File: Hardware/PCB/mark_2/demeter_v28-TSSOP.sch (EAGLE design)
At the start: 68 parts, among them IC1 4050, IC2 LM1117-5.0, IC3 LM1117-3.3, IC5 MCP3424T, IC6 MCP23017SO, IC8 ATMEGA32U4-AU, Q1 IRLML6402, Q2 IRLML6402, Q3 IRLML6402, Q4 IRLML6402, Q5 IRLML6402, Q6 IRLML6402

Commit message: 
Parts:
- R3, R6, R8: value (none) -> 10k
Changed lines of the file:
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@@
 <?xml version="1.0" encoding="utf-8"?>
 <!DOCTYPE eagle SYSTEM "eagle.dtd">
-<eagle version="6.1">
+<eagle version="6.2">
 <drawing>
 <settings>
@@
 <part name="R4" library="mark_2" deviceset="R-EU_" device="R0805"/>
 <part name="GND20" library="mark_2" deviceset="GND" device=""/>
-<part name="R8" library="mark_2" deviceset="R-EU_" device="R0805"/>
+<part name="R8" library="mark_2" deviceset="R-EU_" device="R0805" value="10k"/>
 <part name="D2" library="mark_2" deviceset="MBR0520" device="" value=""/>
 <part name="P+6" library="mark_2" deviceset="+5V" device=""/>
@@
 <part name="JK3" library="mark_2" deviceset="AUDIO-JACK2" device="PTH"/>
 <part name="GND17" library="mark_2" deviceset="GND" device=""/>
-<part name="R6" library="mark_2" deviceset="R-EU_" device="R0805"/>
+<part name="R6" library="mark_2" deviceset="R-EU_" device="R0805" value="10k"/>
 <part name="GND18" library="mark_2" deviceset="GND" device=""/>
 <part name="D6" library="mark_2" deviceset="MBR0520" device="" value=""/>
@@
 <part name="GND8" library="mark_2" deviceset="GND" device=""/>
 <part name="JP1" library="mark_2" deviceset="AVR-ISP-6" device=""/>
-<part name="R3" library="mark_2" deviceset="R-EU_" device="R0805"/>
+<part name="R3" library="mark_2" deviceset="R-EU_" device="R0805" value="10k"/>
 <part name="P+14" library="mark_2" deviceset="+5V" device=""/>
 <part name="P+15" library="mark_2" deviceset="+5V" device=""/>

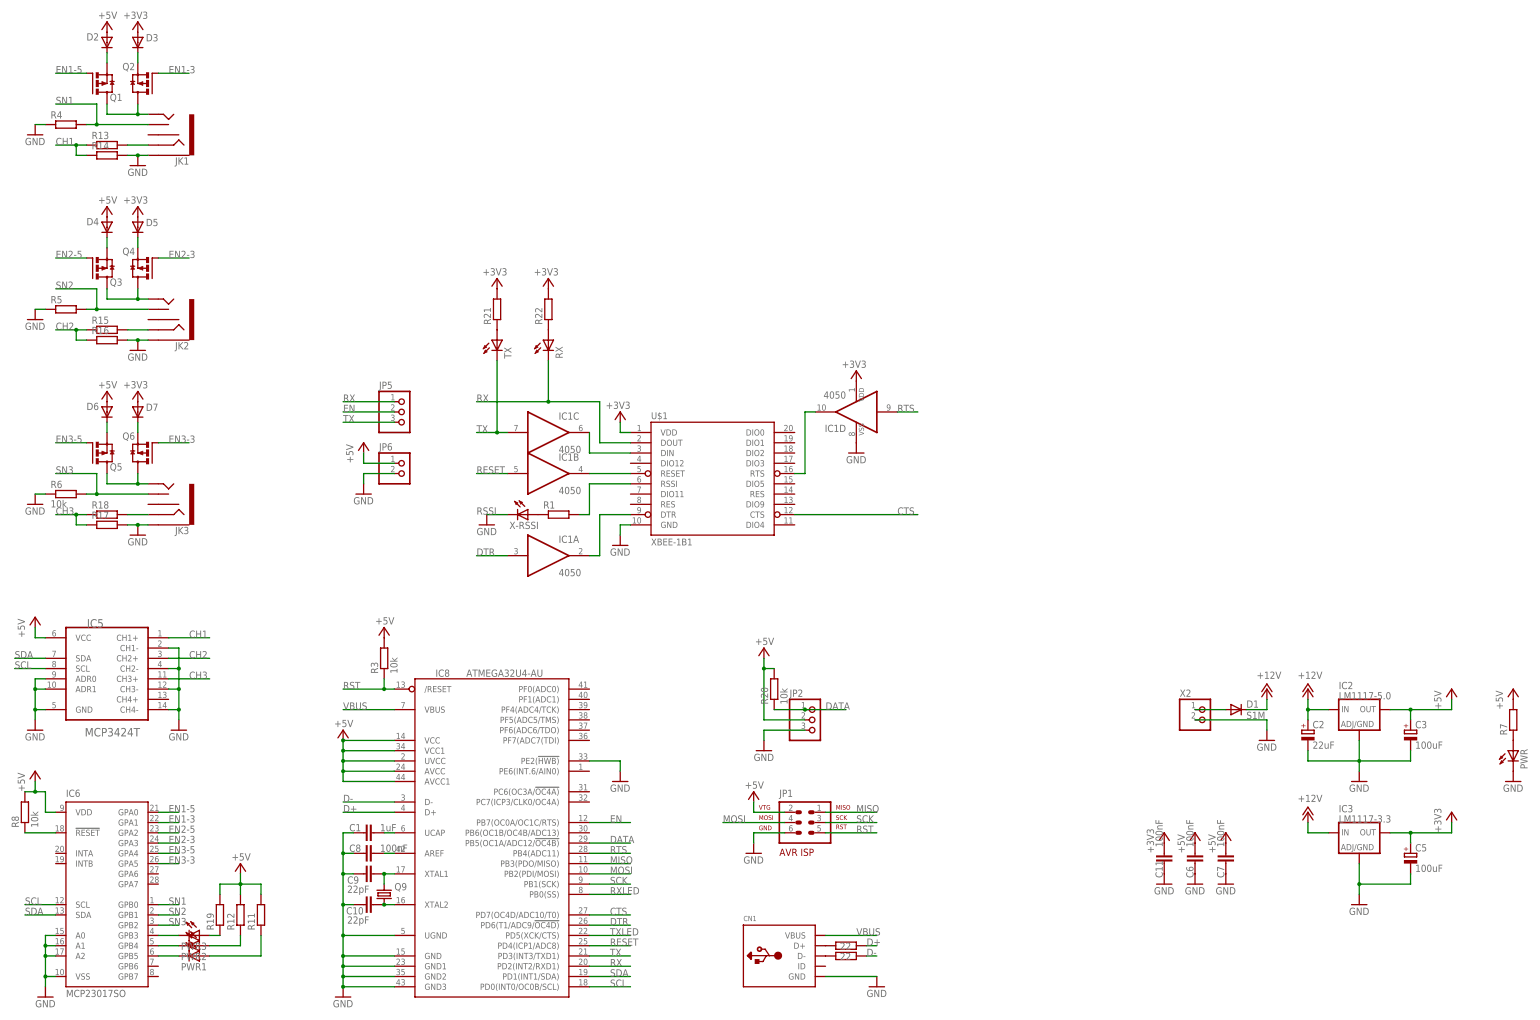
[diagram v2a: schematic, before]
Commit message: 
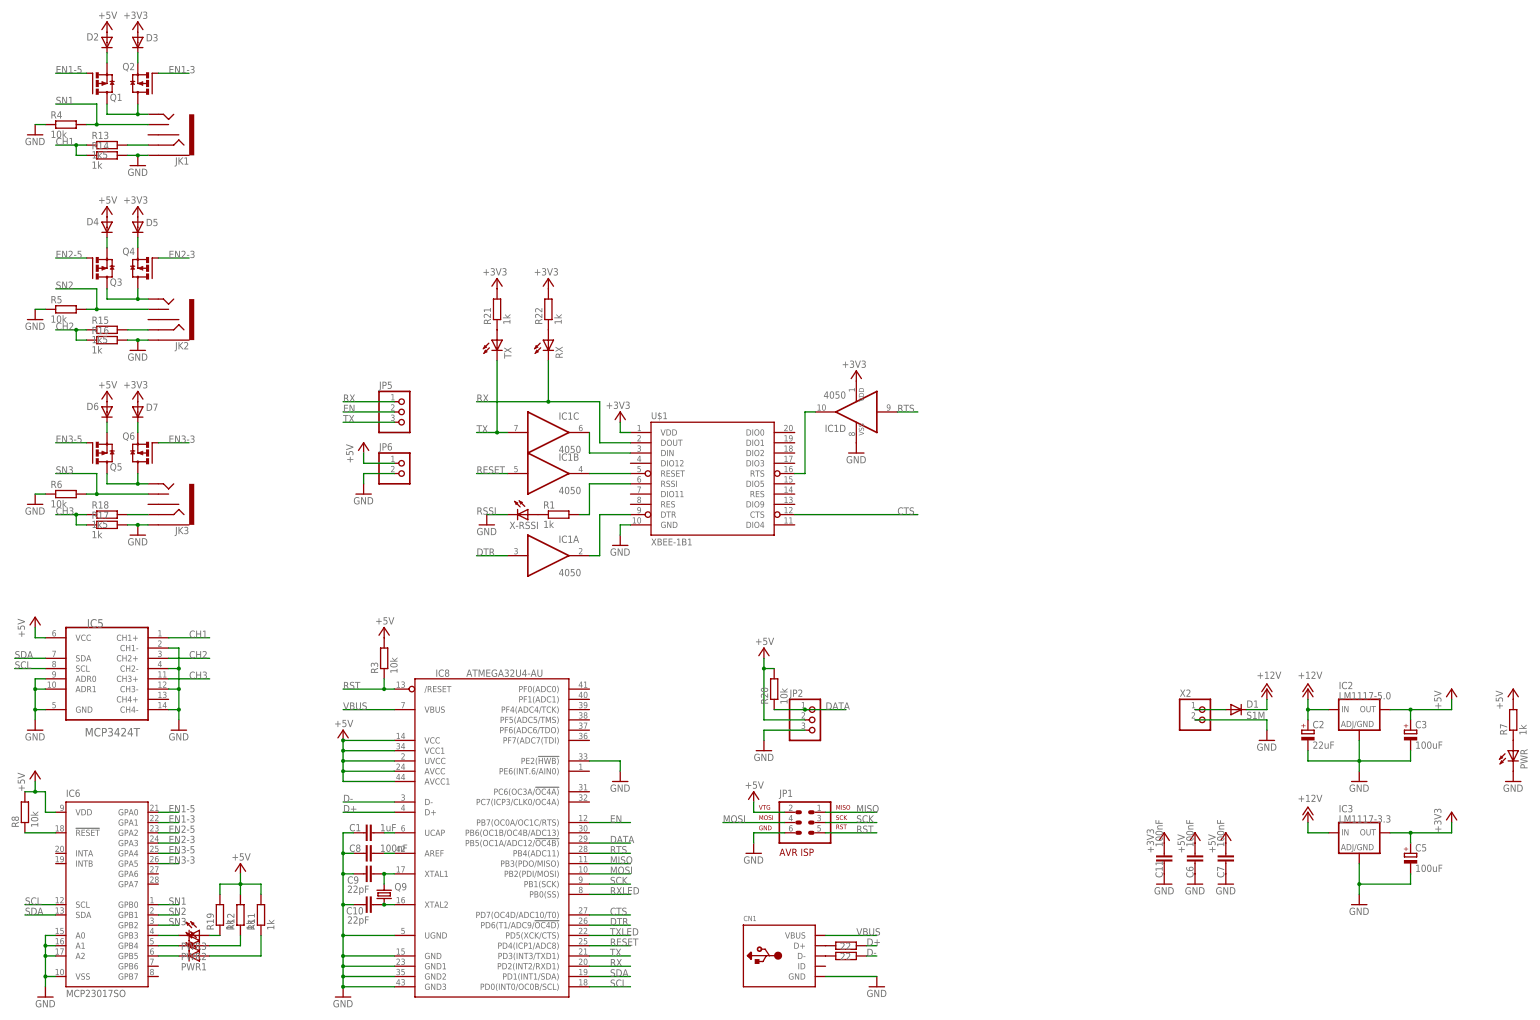
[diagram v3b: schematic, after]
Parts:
- R1, R11, R12, R14, R16, R17, R19, R21, R22, R7: value (none) -> 1k
- R13, R15, R18: value (none) -> 1k5
- R4, R5: value (none) -> 10k
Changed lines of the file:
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@@
 <part name="IC1" library="mark_2" deviceset="4050" device="D" value="4050"/>
 <part name="X-RSSI" library="mark_2" deviceset="LED" device="0805"/>
-<part name="R1" library="mark_2" deviceset="R-EU_" device="R0805"/>
+<part name="R1" library="mark_2" deviceset="R-EU_" device="R0805" value="1k"/>
 <part name="U$1" library="mark_2" deviceset="XBEE-1" device="B1"/>
 <part name="+3V2" library="mark_2" deviceset="+3V3" device=""/>
@@
 <part name="JK1" library="mark_2" deviceset="AUDIO-JACK2" device="PTH"/>
 <part name="GND16" library="mark_2" deviceset="GND" device=""/>
-<part name="R4" library="mark_2" deviceset="R-EU_" device="R0805"/>
+<part name="R4" library="mark_2" deviceset="R-EU_" device="R0805" value="10k"/>
 <part name="GND20" library="mark_2" deviceset="GND" device=""/>
 <part name="R8" library="mark_2" deviceset="R-EU_" device="R0805" value="10k"/>
@@
 <part name="JK2" library="mark_2" deviceset="AUDIO-JACK2" device="PTH"/>
 <part name="GND9" library="mark_2" deviceset="GND" device=""/>
-<part name="R5" library="mark_2" deviceset="R-EU_" device="R0805"/>
+<part name="R5" library="mark_2" deviceset="R-EU_" device="R0805" value="10k"/>
 <part name="GND11" library="mark_2" deviceset="GND" device=""/>
 <part name="D4" library="mark_2" deviceset="MBR0520" device="" value=""/>
@@
 <part name="R9" library="mark_2" deviceset="R-EU_" device="R0805" value="22"/>
 <part name="R10" library="mark_2" deviceset="R-EU_" device="R0805" value="22"/>
-<part name="R13" library="mark_2" deviceset="R-EU_" device="R0805"/>
-<part name="R14" library="mark_2" deviceset="R-EU_" device="R0805"/>
-<part name="R15" library="mark_2" deviceset="R-EU_" device="R0805"/>
-<part name="R16" library="mark_2" deviceset="R-EU_" device="R0805"/>
-<part name="R17" library="mark_2" deviceset="R-EU_" device="R0805"/>
-<part name="R18" library="mark_2" deviceset="R-EU_" device="R0805"/>
+<part name="R13" library="mark_2" deviceset="R-EU_" device="R0805" value="1k5"/>
+<part name="R14" library="mark_2" deviceset="R-EU_" device="R0805" value="1k"/>
+<part name="R15" library="mark_2" deviceset="R-EU_" device="R0805" value="1k5"/>
+<part name="R16" library="mark_2" deviceset="R-EU_" device="R0805" value="1k"/>
+<part name="R17" library="mark_2" deviceset="R-EU_" device="R0805" value="1k"/>
+<part name="R18" library="mark_2" deviceset="R-EU_" device="R0805" value="1k5"/>
 <part name="FRAME1" library="mark_2" deviceset="DINA3_L" device=""/>
 <part name="GND28" library="mark_2" deviceset="GND" device=""/>
@@
 <part name="GND10" library="mark_2" deviceset="GND" device=""/>
 <part name="P+5" library="mark_2" deviceset="+5V" device=""/>
-<part name="R7" library="mark_2" deviceset="R-EU_" device="R0805"/>
+<part name="R7" library="mark_2" deviceset="R-EU_" device="R0805" value="1k"/>
 <part name="PWR" library="mark_2" deviceset="LED" device="0805"/>
 <part name="GND7" library="mark_2" deviceset="GND" device=""/>
@@
 <part name="GND21" library="mark_2" deviceset="GND" device=""/>
 <part name="+3V7" library="mark_2" deviceset="+3V3" device=""/>
-<part name="R11" library="mark_2" deviceset="R-EU_" device="R0805"/>
+<part name="R11" library="mark_2" deviceset="R-EU_" device="R0805" value="1k"/>
 <part name="PWR1" library="mark_2" deviceset="LED" device="0805"/>
 <part name="P+17" library="mark_2" deviceset="+5V" device=""/>
-<part name="R12" library="mark_2" deviceset="R-EU_" device="R0805"/>
+<part name="R12" library="mark_2" deviceset="R-EU_" device="R0805" value="1k"/>
 <part name="PWR2" library="mark_2" deviceset="LED" device="0805"/>
 <part name="PWR3" library="mark_2" deviceset="LED" device="0805"/>
-<part name="R19" library="mark_2" deviceset="R-EU_" device="R0805"/>
+<part name="R19" library="mark_2" deviceset="R-EU_" device="R0805" value="1k"/>
 <part name="P+18" library="mark_2" deviceset="+5V" device=""/>
 <part name="GND25" library="mark_2" deviceset="GND" device=""/>
@@
 <part name="JP2" library="mark_2" deviceset="PINHD-1X3" device="180"/>
 <part name="TX" library="mark_2" deviceset="LED" device="0805"/>
-<part name="R21" library="mark_2" deviceset="R-EU_" device="R0805"/>
+<part name="R21" library="mark_2" deviceset="R-EU_" device="R0805" value="1k"/>
 <part name="RX" library="mark_2" deviceset="LED" device="0805"/>
-<part name="R22" library="mark_2" deviceset="R-EU_" device="R0805"/>
+<part name="R22" library="mark_2" deviceset="R-EU_" device="R0805" value="1k"/>
 <part name="+3V9" library="mark_2" deviceset="+3V3" device=""/>
 <part name="+3V8" library="mark_2" deviceset="+3V3" device=""/>

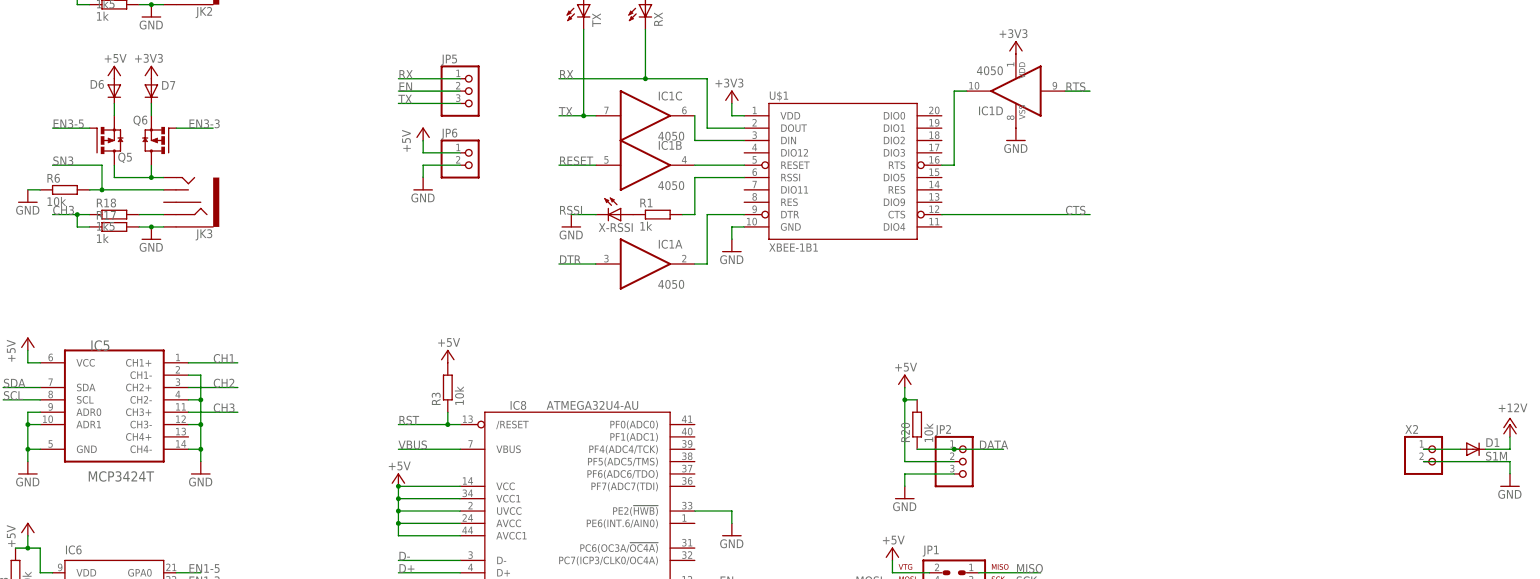
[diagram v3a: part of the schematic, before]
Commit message: 
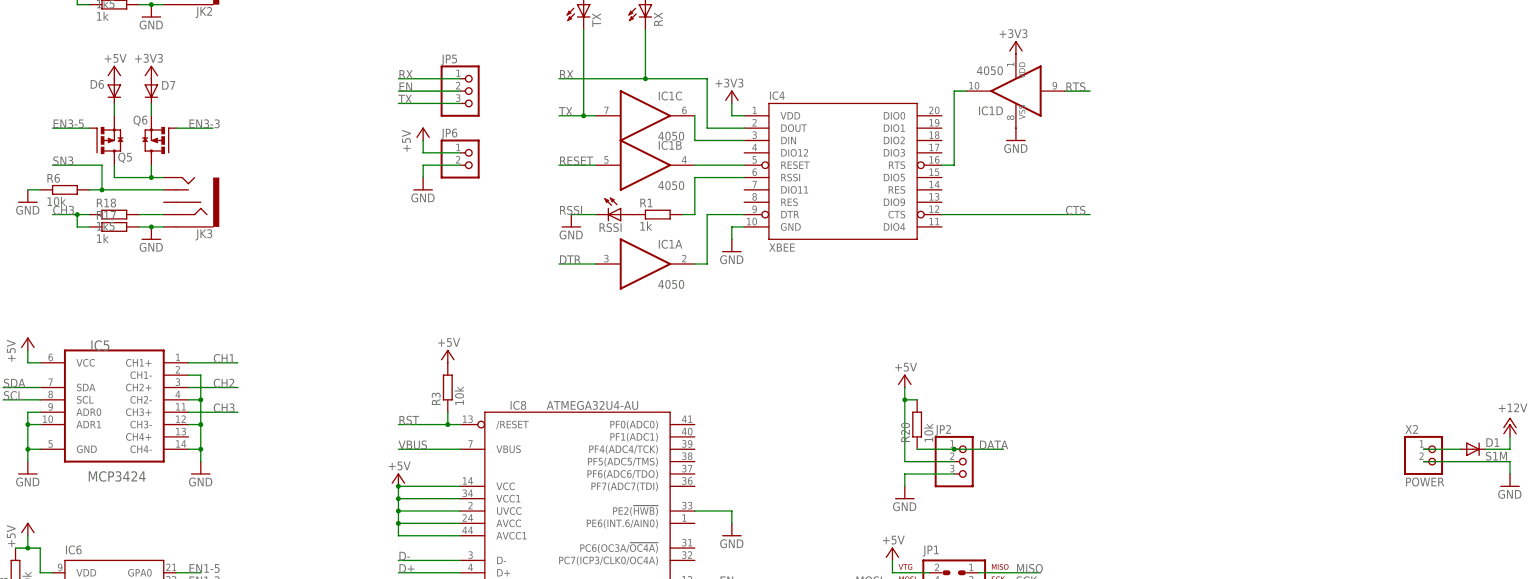
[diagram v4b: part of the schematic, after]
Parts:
- IC4: value XBEE-1B1 -> XBEE
- IC5: value MCP3424T -> MCP3424
- JP1: value AVR-ISP-6 -> AVR-ISP
- X2: value (none) -> POWER
- renumbered U$1 to IC4, X-RSSI to RSSI
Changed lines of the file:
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@@
 <?xml version="1.0" encoding="utf-8"?>
 <!DOCTYPE eagle SYSTEM "eagle.dtd">
-<eagle version="6.2">
+<eagle version="6.1">
 <drawing>
 <settings>
@@
 <parts>
 <part name="IC1" library="mark_2" deviceset="4050" device="D" value="4050"/>
-<part name="X-RSSI" library="mark_2" deviceset="LED" device="0805"/>
+<part name="RSSI" library="mark_2" deviceset="LED" device="0805"/>
 <part name="R1" library="mark_2" deviceset="R-EU_" device="R0805" value="1k"/>
-<part name="U$1" library="mark_2" deviceset="XBEE-1" device="B1"/>
+<part name="IC4" library="mark_2" deviceset="XBEE-1" device="B1" value="XBEE"/>
 <part name="+3V2" library="mark_2" deviceset="+3V3" device=""/>
 <part name="GND3" library="mark_2" deviceset="GND" device=""/>
@@
 <part name="Q1" library="mark_2" deviceset="IRLML6402" device=""/>
 <part name="GND13" library="mark_2" deviceset="GND" device=""/>
-<part name="IC5" library="mark_2" deviceset="MCP3424" device="T"/>
+<part name="IC5" library="mark_2" deviceset="MCP3424" device="T" value="MCP3424"/>
 <part name="P+10" library="mark_2" deviceset="+5V" device=""/>
 <part name="GND14" library="mark_2" deviceset="GND" device=""/>
@@
 <part name="P+13" library="mark_2" deviceset="+5V" device=""/>
 <part name="GND8" library="mark_2" deviceset="GND" device=""/>
-<part name="JP1" library="mark_2" deviceset="AVR-ISP-6" device=""/>
+<part name="JP1" library="mark_2" deviceset="AVR-ISP-6" device="" value="AVR-ISP"/>
 <part name="R3" library="mark_2" deviceset="R-EU_" device="R0805" value="10k"/>
 <part name="P+14" library="mark_2" deviceset="+5V" device=""/>
@@
 <part name="FRAME1" library="mark_2" deviceset="DINA3_L" device=""/>
 <part name="GND28" library="mark_2" deviceset="GND" device=""/>
-<part name="X2" library="mark_2" deviceset="W237-102" device=""/>
+<part name="X2" library="mark_2" deviceset="W237-102" device="" value="POWER"/>
 <part name="GND24" library="mark_2" deviceset="GND" device=""/>
 <part name="JP5" library="mark_2" deviceset="PINHD-1X3" device="180"/>
@@
 <attribute name="VALUE" x="180.34" y="127" size="1.778" layer="96" rot="R180"/>
 </instance>
-<instance part="X-RSSI" gate="G$1" x="101.6" y="96.52" rot="R270"/>
+<instance part="RSSI" gate="G$1" x="101.6" y="96.52" rot="R270"/>
 <instance part="R1" gate="G$1" x="109.22" y="96.52"/>
-<instance part="U$1" gate="G$1" x="147.32" y="106.68"/>
+<instance part="IC4" gate="G$1" x="147.32" y="106.68"/>
 <instance part="+3V2" gate="G$1" x="124.46" y="121.92" smashed="yes">
 <attribute name="VALUE" x="127" y="124.46" size="1.778" layer="96" rot="R180"/>
@@
 <net name="GND" class="0">
 <segment>
-<pinref part="X-RSSI" gate="G$1" pin="C"/>
+<pinref part="RSSI" gate="G$1" pin="C"/>
 <pinref part="GND3" gate="1" pin="GND"/>
 <wire x1="91.44" y1="96.52" x2="96.52" y2="96.52" width="0.1524" layer="91"/>
 </segment>
 <segment>
-<pinref part="U$1" gate="G$1" pin="GND"/>
+<pinref part="IC4" gate="G$1" pin="GND"/>
 <pinref part="GND4" gate="1" pin="GND"/>
 <wire x1="124.46" y1="91.44" x2="124.46" y2="93.98" width="0.1524" layer="91"/>
@@
 <net name="+3V3" class="0">
 <segment>
-<pinref part="U$1" gate="G$1" pin="VDD"/>
+<pinref part="IC4" gate="G$1" pin="VDD"/>
 <pinref part="+3V2" gate="G$1" pin="+3V3"/>
 <wire x1="127" y1="116.84" x2="124.46" y2="116.84" width="0.1524" layer="91"/>
@@
 <net name="N$3" class="0">
 <segment>
-<pinref part="U$1" gate="G$1" pin="DIN"/>
+<pinref part="IC4" gate="G$1" pin="DIN"/>
 <wire x1="116.84" y1="116.84" x2="116.84" y2="111.76" width="0.1524" layer="91"/>
 <wire x1="116.84" y1="111.76" x2="127" y2="111.76" width="0.1524" layer="91"/>
@@
 <net name="N$4" class="0">
 <segment>
-<pinref part="U$1" gate="G$1" pin="RESET"/>
+<pinref part="IC4" gate="G$1" pin="RESET"/>
 <pinref part="IC1" gate="B" pin="O"/>
 <wire x1="116.84" y1="106.68" x2="127" y2="106.68" width="0.1524" layer="91"/>
@@
 <net name="RSSI" class="0">
 <segment>
-<pinref part="U$1" gate="G$1" pin="RSSI"/>
+<pinref part="IC4" gate="G$1" pin="RSSI"/>
 <pinref part="R1" gate="G$1" pin="2"/>
 <wire x1="127" y1="104.14" x2="116.84" y2="104.14" width="0.1524" layer="91"/>
@@
 <segment>
 <pinref part="R1" gate="G$1" pin="1"/>
-<pinref part="X-RSSI" gate="G$1" pin="A"/>
+<pinref part="RSSI" gate="G$1" pin="A"/>
 </segment>
 </net>
@@
 <wire x1="116.84" y1="86.36" x2="119.38" y2="86.36" width="0.1524" layer="91"/>
 <wire x1="119.38" y1="86.36" x2="119.38" y2="96.52" width="0.1524" layer="91"/>
-<pinref part="U$1" gate="G$1" pin="DTR"/>
+<pinref part="IC4" gate="G$1" pin="DTR"/>
 <wire x1="119.38" y1="96.52" x2="127" y2="96.52" width="0.1524" layer="91"/>
 <pinref part="IC1" gate="A" pin="O"/>
@@
 <net name="N$8" class="0">
 <segment>
-<pinref part="U$1" gate="G$1" pin="RTS"/>
+<pinref part="IC4" gate="G$1" pin="RTS"/>
 <wire x1="167.64" y1="106.68" x2="170.18" y2="106.68" width="0.1524" layer="91"/>
 <wire x1="170.18" y1="106.68" x2="170.18" y2="121.92" width="0.1524" layer="91"/>
@@
 <net name="CTS" class="0">
 <segment>
-<pinref part="U$1" gate="G$1" pin="CTS"/>
+<pinref part="IC4" gate="G$1" pin="CTS"/>
 <wire x1="167.64" y1="96.52" x2="198.12" y2="96.52" width="0.1524" layer="91"/>
 <label x="193.04" y="96.52" size="1.778" layer="95"/>
@@
 </segment>
 <segment>
-<pinref part="U$1" gate="G$1" pin="DOUT"/>
+<pinref part="IC4" gate="G$1" pin="DOUT"/>
 <wire x1="127" y1="114.3" x2="119.38" y2="114.3" width="0.1524" layer="91"/>
 <wire x1="119.38" y1="114.3" x2="119.38" y2="124.46" width="0.1524" layer="91"/>
